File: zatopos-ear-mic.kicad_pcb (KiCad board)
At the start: 2 copper layers, 80 x 40 mm, 25 parts, among them J2 Conn_01x06_Socket, U1 NJU7043, U2 MCP3002

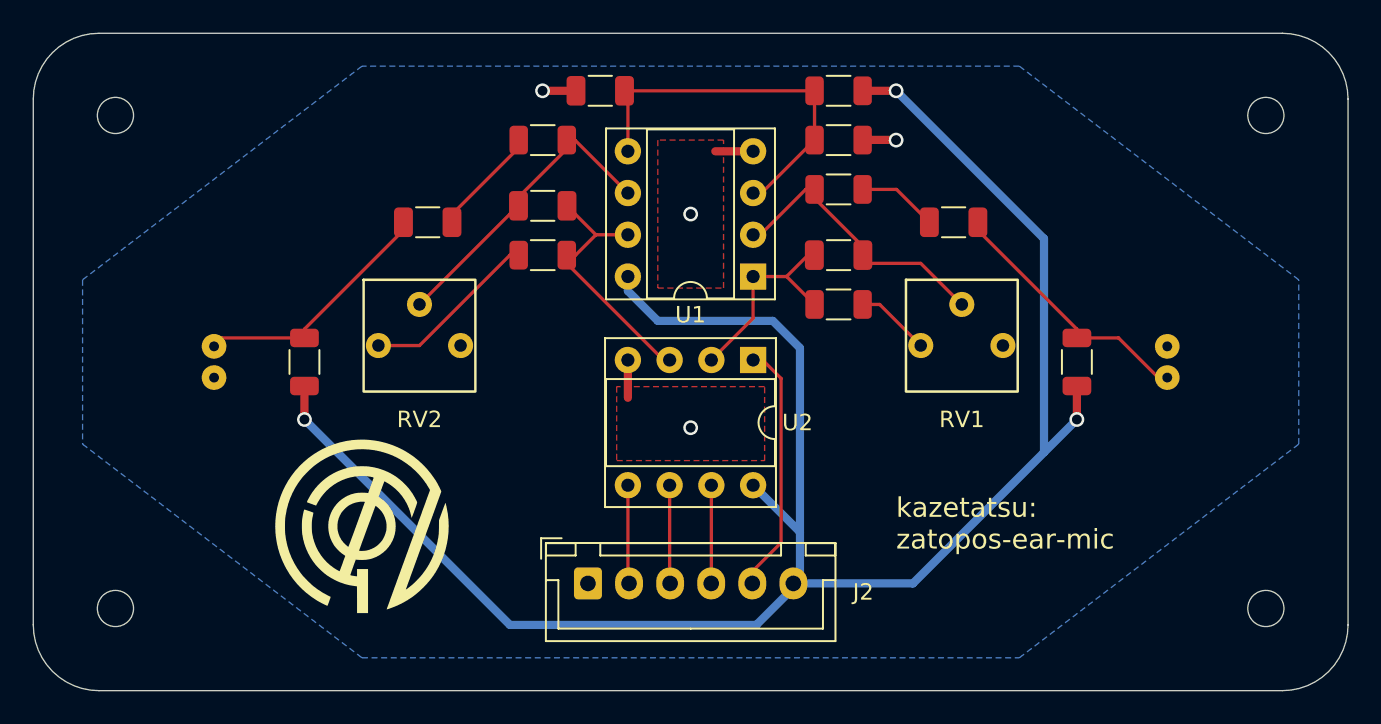
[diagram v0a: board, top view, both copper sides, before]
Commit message: Change wire, place: shorter path & less corner
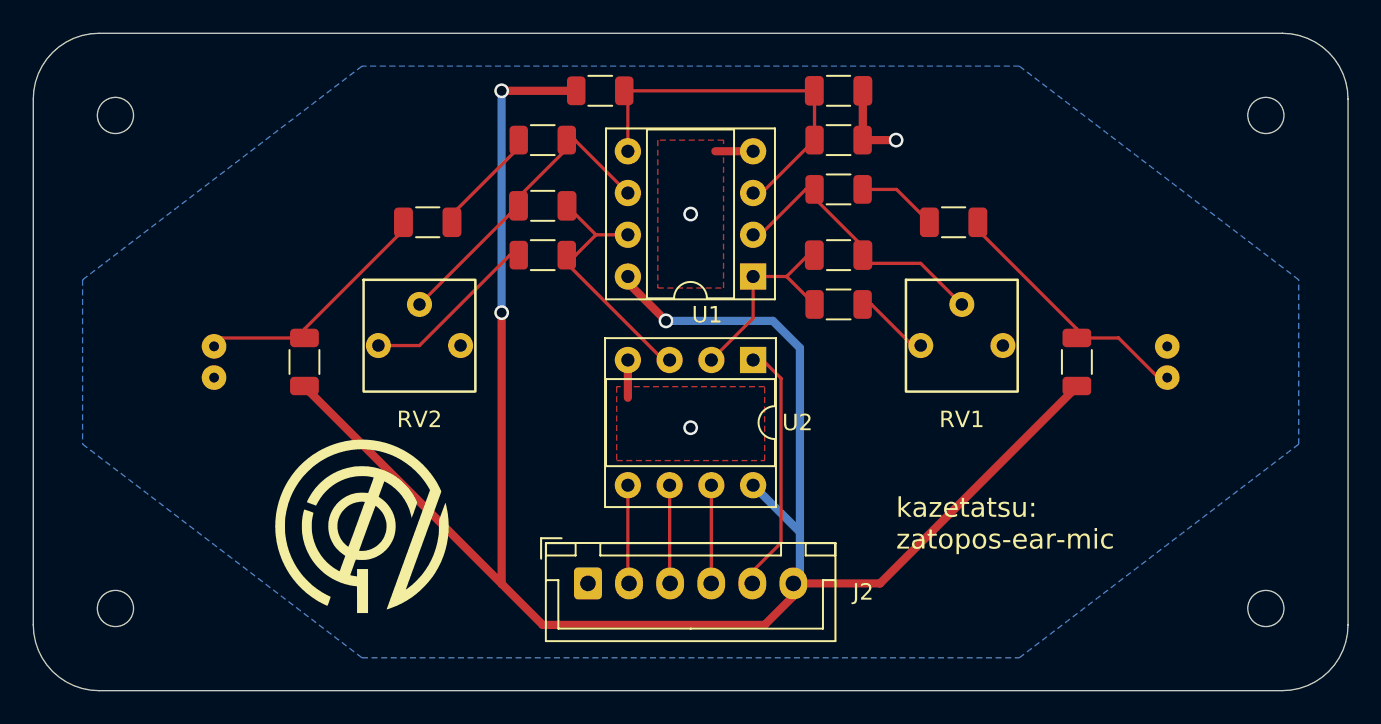
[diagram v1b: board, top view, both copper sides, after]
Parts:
- moved C5 14.5 mm to (159.0, 83.5), turned to 0 degrees
- moved R7 14.5 mm to (144.5, 83.5), turned to 0 degrees
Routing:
- net +3.3V: track 120.7 -> 125.3 mm
- net GND: track 8.67 -> 9.64 mm, vias 4 -> 3

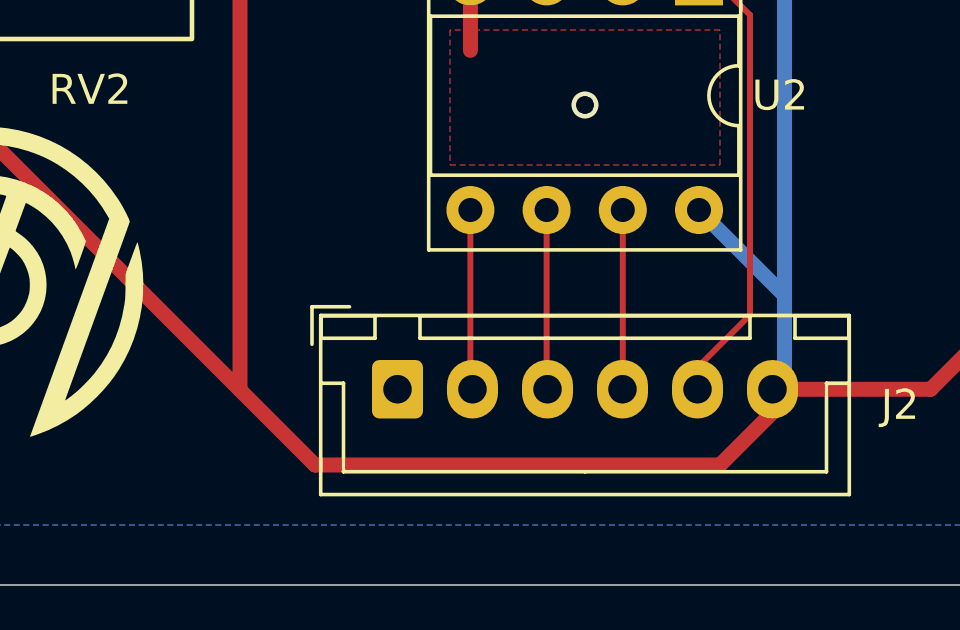
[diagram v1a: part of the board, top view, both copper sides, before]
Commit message: Change wire, place: less corner
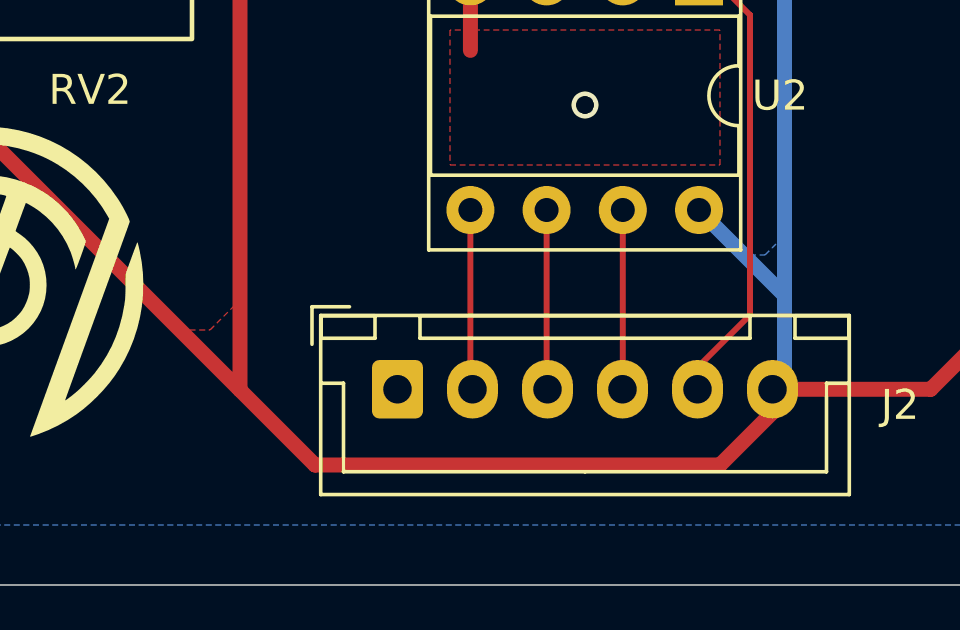
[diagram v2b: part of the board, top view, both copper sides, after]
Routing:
- added copper zone on B.Cu, net +3.3V
- added copper zone on F.Cu, net +3.3V
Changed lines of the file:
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@@
 		(tags "resistor")
 		(property "Reference" "R7"
-			(at 0 -1.82 360)
+			(at 0 -1.82 0)
 			(layer "F.SilkS")
 			(hide yes)
@@
 		)
 		(property "Value" "100k"
-			(at 0 1.82 360)
+			(at 0 1.82 0)
 			(layer "F.Fab")
 			(effects
@@
 		)
 		(fp_text user "${REFERENCE}"
-			(at 0 0 360)
+			(at 0 0 0)
 			(layer "F.Fab")
 			(effects
@@
 		(tags "capacitor")
 		(property "Reference" "C5"
-			(at 0 -1.85 360)
+			(at 0 -1.85 0)
 			(layer "F.SilkS")
 			(hide yes)
@@
 		)
 		(property "Value" "1u"
-			(at 0 1.85 360)
+			(at 0 1.85 0)
 			(layer "F.Fab")
 			(effects
@@
 		)
 		(fp_text user "${REFERENCE}"
-			(at 0 0 360)
+			(at 0 0 0)
 			(layer "F.Fab")
 			(effects
@@
 	)
 	(zone
+		(net 14)
+		(net_name "+3.3V")
+		(layer "F.Cu")
+		(hatch edge 0.5)
+		(priority 3)
+		(connect_pads
+			(clearance 0.5)
+		)
+		(min_thickness 0.25)
+		(filled_areas_thickness no)
+		(fill yes
+			(thermal_gap 0.5)
+			(thermal_bridge_width 0.5)
+		)
+		(polygon
+			(pts
+				(xy 138.5 113.5) (xy 136.5 111.5) (xy 137.5 111.5) (xy 138.5 110.5)
+			)
+		)
+	)
+	(zone
 		(net 9)
 		(net_name "GND")
@@
 			)
 		)
+	)
+	(zone
+		(net 14)
+		(net_name "+3.3V")
+		(layer "B.Cu")
+		(hatch edge 0.5)
+		(priority 4)
+		(connect_pads
+			(clearance 0.5)
+		)
+		(min_thickness 0.25)
+		(filled_areas_thickness no)
+		(fill yes
+			(thermal_gap 0.5)
+			(thermal_bridge_width 0.5)
+		)
+		(polygon
+			(pts
+				(xy 156.5 110) (xy 155.5 109) (xy 156 109) (xy 156.5 108.5)
+			)
+		)
